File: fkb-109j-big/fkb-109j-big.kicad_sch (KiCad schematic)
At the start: 187 parts

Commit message: start board layout
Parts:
- added D100, D106, D107, D109, D110, D111, D112, D80, D81, D83, D84, D85, D86, D87, D88, D89, D94, D95: 1N4148, Diode_THT:D_DO-35_SOD27_P7.62mm_Horizontal, symbol Diode:1N4148
- added MX_CPSLK1, MX_LSUPR1, MX_RSUPR1: MX-NoLED, Alps_Only:ALPS-1.5U, symbol MX_Alps_Hybrid:MX-NoLED
- added MX_KP0, MX_KP1, MX_KP2, MX_KP3, MX_KP4, MX_KP5, MX_KP6, MX_KP7, MX_KP8, MX_KP9, MX_KPAST1, MX_KPDOT1, MX_KPEQ1, MX_KPFSL1, MX_KPMNS1, MX_KPPLS1, MX_NMLK1: MX-NoLED, Alps_Only:ALPS-1U, symbol MX_Alps_Hybrid:MX-NoLED
- added MX_KPENT1: MX-NoLED, Alps_Only:ALPS-2U, symbol MX_Alps_Hybrid:MX-NoLED
- added MX_LCTRL1, MX_LOPT1, MX_RCTRL1, MX_ROPT1: MX-NoLED, Alps_Only:ALPS-1.25U, symbol MX_Alps_Hybrid:MX-NoLED
- added MX_RSHFT1: MX-NoLED, Alps_Only:ALPS-2.75U, symbol MX_Alps_Hybrid:MX-NoLED
- added MX_RTRN1: MX-NoLED, Alps_Only:ALPS-2.25U, symbol MX_Alps_Hybrid:MX-NoLED
- added MX_SPACE1: MX-NoLED, Alps_Only:ALPS-6.5U, symbol MX_Alps_Hybrid:MX-NoLED
- added MX_SPACE2: MX-NoLED, Alps_Only:ALPS-6.25U, symbol MX_Alps_Hybrid:MX-NoLED
- added R1, R10, R11, R12, R13, R14, R15, R16, R17, R18, R19, R2, R20, R21, R22, R23, R24, R25, R26, R3, R4, R5, R6, R7, R8, R9: R, Resistor_THT:R_Axial_DIN0207_L6.3mm_D2.5mm_P10.16mm_Horizontal, symbol Device:R
- MX_0, MX_1, MX_2, MX_3, MX_4, MX_5, MX_6, MX_7, MX_8, MX_9, MX_F1, MX_F10, MX_F11, MX_F12, MX_F2, MX_F3, MX_F4, MX_F5, MX_F6, MX_F7, MX_F8, MX_F9, MX_KC27, MX_KC28, MX_KC33, MX_KC34, MX_KC35, MX_KC73: footprint (none) -> Alps_Only:ALPS-1U
- MX_A1: renamed from MX_A; footprint (none) -> Alps_Only:ALPS-1U
- MX_B1: renamed from MX_B; footprint (none) -> Alps_Only:ALPS-1U
- MX_BS2: renamed from MX_BS1; footprint Alps_Only:ALPS-1U -> Alps_Only:ALPS-2U
- MX_BSLSH1: renamed from MX_BSLSH; footprint (none) -> Alps_Only:ALPS-1.5U
- MX_C1: renamed from MX_C; footprint (none) -> Alps_Only:ALPS-1U
- MX_CPSLK2: renamed from MX_CPSLK; footprint (none) -> Alps_Only:ALPS-1.75U
- MX_D1: renamed from MX_D; footprint (none) -> Alps_Only:ALPS-1U
- MX_DEL1: renamed from MX_DEL; footprint (none) -> Alps_Only:ALPS-1U
- MX_DOWN1: renamed from MX_DOWN; footprint (none) -> Alps_Only:ALPS-1U
- MX_E1: renamed from MX_E; footprint (none) -> Alps_Only:ALPS-1U
- MX_END1: renamed from MX_END; footprint (none) -> Alps_Only:ALPS-1U
- MX_ENTR1: renamed from MX_ENTR; footprint (none) -> Alps_Only:ALPS-2U
- MX_ESC1: renamed from MX_ESC; footprint (none) -> Alps_Only:ALPS-1U
- MX_F13: renamed from MX_F; footprint (none) -> Alps_Only:ALPS-1U
- MX_G1: renamed from MX_G; footprint (none) -> Alps_Only:ALPS-1U
- MX_H1: renamed from MX_H; footprint (none) -> Alps_Only:ALPS-1U
- MX_HOME1: renamed from MX_HOME; footprint (none) -> Alps_Only:ALPS-1U
- MX_I1: renamed from MX_I; footprint (none) -> Alps_Only:ALPS-1U
- MX_INS1: renamed from MX_INS; footprint (none) -> Alps_Only:ALPS-1U
- MX_J1: renamed from MX_J; footprint (none) -> Alps_Only:ALPS-1U
- MX_K1: renamed from MX_K; footprint (none) -> Alps_Only:ALPS-1U
- MX_KC0C1: renamed from MX_KC0C; footprint (none) -> Alps_Only:ALPS-1U
- MX_KC0D1: renamed from MX_KC0D; footprint (none) -> Alps_Only:ALPS-1U
- MX_KC1A1: renamed from MX_KC1A; footprint (none) -> Alps_Only:ALPS-1U
- MX_KC1B1: renamed from MX_KC1B; footprint (none) -> Alps_Only:ALPS-1U
- MX_KC2B1: renamed from MX_KC2B; footprint (none) -> Alps_Only:ALPS-1U
- MX_KC70, MX_KC79: footprint (none) -> Alps_Only:ALPS-1.25U
- MX_KC7B1: renamed from MX_KC7B; footprint (none) -> Alps_Only:ALPS-1.25U
- MX_KC7D1: renamed from MX_KC7D; footprint (none) -> Alps_Only:ALPS-1U
- MX_L1: renamed from MX_L; footprint (none) -> Alps_Only:ALPS-1U
- MX_LALT1: renamed from MX_LALT; footprint (none) -> Alps_Only:ALPS-1.25U
- MX_LCTRL2: renamed from MX_LCTRL; footprint (none) -> Alps_Only:ALPS-1.5U
- MX_LEFT1: renamed from MX_LEFT; footprint (none) -> Alps_Only:ALPS-1U
- MX_LSHFT1: renamed from MX_LSHFT; footprint (none) -> Alps_Only:ALPS-2.25U
- MX_LWIN1: renamed from MX_LWIN; footprint (none) -> Alps_Only:ALPS-1.25U
- MX_M1: renamed from MX_M; footprint (none) -> Alps_Only:ALPS-1U
- MX_MENU1: renamed from MX_MENU; footprint (none) -> Alps_Only:ALPS-1.25U
- MX_N1: renamed from MX_N; footprint (none) -> Alps_Only:ALPS-1U
- MX_O1: renamed from MX_O; footprint (none) -> Alps_Only:ALPS-1U
- MX_P1: renamed from MX_P; footprint (none) -> Alps_Only:ALPS-1U
- MX_PGDN1: renamed from MX_PGDN; footprint (none) -> Alps_Only:ALPS-1U
- MX_PGUP1: renamed from MX_PGUP; footprint (none) -> Alps_Only:ALPS-1U
- MX_PSBRK1: renamed from MX_PSBRK; footprint (none) -> Alps_Only:ALPS-1U
- MX_PSCRN1: renamed from MX_PSCRN; footprint (none) -> Alps_Only:ALPS-1U
- MX_Q1: renamed from MX_Q; footprint (none) -> Alps_Only:ALPS-1U
- MX_R1: renamed from MX_R; footprint (none) -> Alps_Only:ALPS-1U
- MX_RALT1: renamed from MX_RALT; footprint (none) -> Alps_Only:ALPS-1.25U
- MX_RCTRL2: renamed from MX_CTRL; footprint (none) -> Alps_Only:ALPS-1.5U
- MX_RGHT1: renamed from MX_RGHT; footprint (none) -> Alps_Only:ALPS-1U
- MX_RSHFT2: renamed from MX_RSHFT; footprint (none) -> Alps_Only:ALPS-1.75U
- MX_RWIN1: renamed from MX_RWIN; footprint (none) -> Alps_Only:ALPS-1.25U
- MX_S1: renamed from MX_S; footprint (none) -> Alps_Only:ALPS-1U
- MX_SCRLK1: renamed from MX_SCRLK; footprint (none) -> Alps_Only:ALPS-1U
- MX_SPACE3: renamed from MX_SPACE; footprint (none) -> Alps_Only:ALPS-2.5U
- MX_T1: renamed from MX_T; footprint (none) -> Alps_Only:ALPS-1U
- MX_TAB1: renamed from MX_TAB; footprint (none) -> Alps_Only:ALPS-1.5U
- MX_TILDE1: renamed from MX_TILDE; footprint (none) -> Alps_Only:ALPS-1U
- MX_U1: renamed from MX_U; footprint (none) -> Alps_Only:ALPS-1U
- MX_UP1: renamed from MX_UP; footprint (none) -> Alps_Only:ALPS-1U
- MX_V1: renamed from MX_V; footprint (none) -> Alps_Only:ALPS-1U
- MX_W1: renamed from MX_W; footprint (none) -> Alps_Only:ALPS-1U
- MX_X1: renamed from MX_X; footprint (none) -> Alps_Only:ALPS-1U
- MX_Y1: renamed from MX_Y; footprint (none) -> Alps_Only:ALPS-1U
- MX_Z1: renamed from MX_Z; footprint (none) -> Alps_Only:ALPS-1U
- renumbered MX_BS2 to MX_BS1
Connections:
- net COL2: now reaches MX_S1.1 (COL)
- net COL2: now also MX_2.1 (COL), MX_LALT1.1 (COL), MX_W1.1 (COL), MX_X1.1 (COL), MX_LSUPR1.2 (ROW), R2.2
- net at D97.1 (K): now also D103.1 (K), D91.1 (K), R17.2
- net ROW4: now reaches D53.1 (K)
- net ROW4: now also D17.1 (K), D19.1 (K), D21.1 (K), D23.1 (K), D29.1 (K), D35.1 (K), D41.1 (K), D47.1 (K), D59.1 (K), D65.1 (K), D71.1 (K), D77.1 (K), D82.1 (K), R20.1
- net COL9: now reaches MX_O1.1 (COL)
- net COL9: now also MX_9.1 (COL), MX_KC34.1 (COL), MX_L1.1 (COL), MX_MENU1.1 (COL), MX_ROPT1.2 (ROW), R9.2
- net ROW5: now reaches D24.1 (K)
- net ROW5: now also D18.1 (K), D20.1 (K), D22.1 (K), D30.1 (K), D36.1 (K), D42.1 (K), D48.1 (K), D54.1 (K), D60.1 (K), D66.1 (K), R22.1
- net ROW3: now reaches D34.1 (K)
- net ROW3: now also D10.1 (K), D12.1 (K), D14.1 (K), D16.1 (K), D28.1 (K), D40.1 (K), D46.1 (K), D52.1 (K), D58.1 (K), D64.1 (K), D70.1 (K), D72.1 (K), D76.1 (K), R21.1
- net COL13: now reaches MX_BS1.1 (COL), MX_BS2.1 (COL)
- net COL13: now also MX_BSLSH1.1 (COL), MX_ENTR1.1 (COL), MX_KC7D1.1 (COL), MX_RTRN1.1 (COL), R13.2
- net ROW1: now reaches D68.1 (K)
- net ROW1: now also D26.1 (K), D32.1 (K), D38.1 (K), D44.1 (K), D5.1 (K), D50.1 (K), D56.1 (K), D6.1 (K), D62.1 (K), D7.1 (K), D74.1 (K), D79.1 (K), D8.1 (K), R18.1
- net COL10: now reaches MX_P1.1 (COL)
- net COL10: now also MX_0.1 (COL), MX_KC27.1 (COL), MX_KC35.1 (COL), MX_RCTRL2.1 (COL), MX_RCTRL1.1 (COL), R10.2
- net ROW0: now reaches D3.1 (K)
- net ROW0: now also D1.1 (K), D2.1 (K), D25.1 (K), D31.1 (K), D37.1 (K), D4.1 (K), D43.1 (K), D49.1 (K), D55.1 (K), D61.1 (K), D67.1 (K), D73.1 (K), R17.1
- net COL11: now reaches MX_KC73.1 (COL)
- net COL11: now also MX_KC0C1.1 (COL), MX_KC1A1.1 (COL), MX_KC28.1 (COL), R11.2
- net at MX_F6.1 (COL): now also R7.1
- net ROW2: now reaches D13.1 (K)
- net ROW2: now also D11.1 (K), D15.1 (K), D27.1 (K), D33.1 (K), D39.1 (K), D45.1 (K), D51.1 (K), D57.1 (K), D63.1 (K), D69.1 (K), D75.1 (K), D78.1 (K), D9.1 (K), R19.1
- net COL7: now reaches MX_U1.1 (COL)
- net COL7: now also MX_7.1 (COL), MX_J1.1 (COL), MX_M1.1 (COL), MX_RALT1.1 (COL), R7.2
- net at D96.1 (K): now also D102.1 (K), D108.1 (K), R22.2, R26.1
- net COL4: now reaches MX_V1.1 (COL)
- net COL4: now also MX_4.1 (COL), MX_F13.1 (COL), MX_R1.1 (COL), MX_SPACE3.1 (COL), MX_SPACE1.1 (COL), MX_SPACE2.1 (COL), R4.2
- net at D20.2 (A), MX_LWIN1.2 (ROW): now also MX_LOPT1.1 (COL)
- net COL1: now reaches MX_LWIN1.1 (COL)
- net COL1: now also MX_1.1 (COL), MX_A1.1 (COL), MX_Q1.1 (COL), MX_Z1.1 (COL), MX_LOPT1.2 (ROW)
- net COL6: now reaches MX_H1.1 (COL)
- net COL6: now also MX_6.1 (COL), MX_KC70.1 (COL), MX_N1.1 (COL), MX_Y1.1 (COL), R6.2
- net at D30.2 (A), MX_SPACE3.2 (ROW): now also MX_SPACE1.2 (ROW), MX_SPACE2.2 (ROW)
- net COL0: now reaches MX_TAB1.1 (COL)
- net COL0: now also MX_CPSLK2.1 (COL), MX_LCTRL2.1 (COL), MX_LSHFT1.1 (COL), MX_TILDE1.1 (COL), MX_CPSLK1.1 (COL), MX_LCTRL1.1 (COL), R1.2
- net at D93.1 (K): now also D105.1 (K), D99.1 (K), R19.2, R24.1
- net COL8: now reaches MX_I1.1 (COL)
- net COL8: now also MX_8.1 (COL), MX_K1.1 (COL), MX_KC33.1 (COL), MX_RWIN1.1 (COL), MX_RSUPR1.2 (ROW), R8.2
- net at D82.2 (A), MX_ENTR1.2 (ROW): now also MX_RTRN1.2 (ROW)
- net COL5: now reaches MX_5.1 (COL)
- net COL5: now also MX_B1.1 (COL), MX_G1.1 (COL), MX_KC79.1 (COL), MX_T1.1 (COL), R5.2
- net COL12: now reaches MX_KC0D1.1 (COL)
- net COL12: now also MX_KC1B1.1 (COL), MX_KC2B1.1 (COL), MX_RSHFT2.1 (COL), MX_RSHFT1.1 (COL), R12.2
- net at MX_MENU1.2 (ROW): now also D60.2 (A), MX_ROPT1.1 (COL); no longer D48.2 (A)
- net at D77.2 (A), MX_RSHFT2.2 (ROW): now also MX_RSHFT1.2 (ROW)
- net at D22.2 (A), MX_LALT1.2 (ROW): now also MX_LSUPR1.1 (COL)
- net at MX_PSCRN1.1 (COL): now also R14.1
- net at D54.2 (A), MX_RWIN1.2 (ROW): now also MX_RSUPR1.1 (COL)
- net at MX_F12.1 (COL): now also R13.1
- net at MX_F5.1 (COL): now also R6.1
- net COL14: now reaches MX_DEL1.1 (COL)
- net COL14: now also MX_INS1.1 (COL), MX_LEFT1.1 (COL), R14.2
- net at MX_F10.1 (COL): now also R11.1
- net at D98.1 (K): now also D104.1 (K), D92.1 (K), R18.2, R23.1
- net at MX_F4.1 (COL): now also R5.1
- net at D18.2 (A), MX_LCTRL2.2 (ROW): now also MX_LCTRL1.2 (ROW)
- net at MX_F8.1 (COL): now also R9.1
- net at MX_ESC1.1 (COL): now also R1.1
- net at MX_F7.1 (COL): now also R8.1
- net COL16: now reaches MX_PGDN1.1 (COL)
- net COL16: now also MX_PGUP1.1 (COL), MX_RGHT1.1 (COL), R16.2
- net at D66.2 (A), MX_RCTRL2.2 (ROW): now also MX_RCTRL1.2 (ROW)
- net at MX_F9.1 (COL): now also R10.1
- net at MX_RALT1.2 (ROW): now also D48.2 (A); no longer D60.2 (A)
- net COL15: now reaches MX_HOME1.1 (COL)
- net COL15: now also MX_DOWN1.1 (COL), MX_END1.1 (COL), MX_UP1.1 (COL), R15.2
- net at D101.1 (K): now also R20.2, R25.1
- net at MX_SCRLK1.1 (COL): now also R15.1
- net COL3: now reaches MX_KC7B1.1 (COL)
- net COL3: now also MX_3.1 (COL), MX_C1.1 (COL), MX_D1.1 (COL), MX_E1.1 (COL), R3.2
- net at MX_F1.1 (COL): now also R2.1
- net at MX_F3.1 (COL): now also R4.1
- net at MX_F11.1 (COL): now also R12.1
- net at D10.2 (A), MX_CPSLK2.2 (ROW): now also MX_CPSLK1.2 (ROW)
- net at MX_F2.1 (COL): now also R3.1
- net at MX_PSBRK1.1 (COL): now also R16.1
- new net: D100.1 (K), D111.1 (K), D83.1 (K), D88.1 (K), R21.2
- new net: D106.1 (K), D112.1 (K), D84.1 (K), D89.1 (K), R25.2
- new net: D84.2 (A), MX_KP1.2 (ROW)
- new net: D81.2 (A), MX_KP7.2 (ROW)
- new net: D109.1 (K), D80.1 (K), D86.1 (K), D94.1 (K), R23.2
- new net: D89.2 (A), MX_KP2.2 (ROW)
- new net: D107.2 (A), MX_KPDOT1.2 (ROW)
- new net: D80.2 (A), MX_NMLK1.2 (ROW)
- new net: D107.1 (K), D85.1 (K), R26.2
- new net: D85.2 (A), MX_KP0.2 (ROW)
- new net: D110.1 (K), D81.1 (K), D87.1 (K), D95.1 (K), R24.2
- new net: D110.2 (A), MX_KPMNS1.2 (ROW)
- new net: D112.2 (A), MX_KPENT1.2 (ROW)
- new net: D86.2 (A), MX_KPEQ1.2 (ROW)
- new net: D88.2 (A), MX_KP5.2 (ROW)
- new net: D111.2 (A), MX_KPPLS1.2 (ROW)
- new net: D83.2 (A), MX_KP4.2 (ROW)
- new net: D95.2 (A), MX_KP9.2 (ROW)
- new net: D100.2 (A), MX_KP6.2 (ROW)
- new net: D94.2 (A), MX_KPFSL1.2 (ROW)
- new net: D87.2 (A), MX_KP8.2 (ROW)
- new net: D109.2 (A), MX_KPAST1.2 (ROW)
- new net: D106.2 (A), MX_KP3.2 (ROW)
- new net COL17: MX_KP0.1 (COL), MX_KP1.1 (COL), MX_KP4.1 (COL), MX_KP7.1 (COL), MX_NMLK1.1 (COL)
- new net COL18: MX_KP2.1 (COL), MX_KP5.1 (COL), MX_KP8.1 (COL), MX_KPEQ1.1 (COL)
- new net COL19: MX_KP3.1 (COL), MX_KP6.1 (COL), MX_KP9.1 (COL), MX_KPDOT1.1 (COL), MX_KPFSL1.1 (COL)
- new net COL20: MX_KPAST1.1 (COL), MX_KPENT1.1 (COL), MX_KPMNS1.1 (COL), MX_KPPLS1.1 (COL)
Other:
- moved on the sheet: D101, D102, D108, D2, D25, D3, D31, D37, D4, D43, D49, D55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

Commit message: continue layout
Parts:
- added MX_KPPLS2: MX-NoLED, Alps_Only:ALPS-2U, symbol MX_Alps_Hybrid:MX-NoLED
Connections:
- net COL20: now also MX_KPPLS2.1 (COL)
- net at D111.2 (A), MX_KPPLS1.2 (ROW): now also MX_KPPLS2.2 (ROW)
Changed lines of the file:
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@@
   (junction (at 86.36 138.43) (diameter 0) (color 0 0 0 0)
   )
+  (junction (at 307.34 102.87) (diameter 0) (color 0 0 0 0)
+  )
   (junction (at 193.04 105.41) (diameter 0) (color 0 0 0 0)
   )
@@
   (junction (at 40.64 125.73) (diameter 0) (color 0 0 0 0)
   )
+  (junction (at 302.26 110.49) (diameter 0) (color 0 0 0 0)
+  )
   (junction (at 231.14 85.09) (diameter 0) (color 0 0 0 0)
   )
@@
     (stroke (width 0) (type default))
   )
-  (wire (pts (xy 307.34 85.09) (xy 307.34 105.41))
+  (wire (pts (xy 307.34 85.09) (xy 307.34 102.87))
     (stroke (width 0) (type default))
   )
@@
     (stroke (width 0) (type default))
   )
+  (wire (pts (xy 299.72 107.95) (xy 299.72 110.49))
+    (stroke (width 0) (type default))
+  )
   (wire (pts (xy 25.4 102.87) (xy 27.94 102.87))
     (stroke (width 0) (type default))
@@
     (stroke (width 0) (type default))
   )
+  (wire (pts (xy 304.8 102.87) (xy 307.34 102.87))
+    (stroke (width 0) (type default))
+  )
   (wire (pts (xy 40.64 140.97) (xy 40.64 146.05))
     (stroke (width 0) (type default))
@@
     (stroke (width 0) (type default))
   )
+  (wire (pts (xy 299.72 110.49) (xy 302.26 110.49))
+    (stroke (width 0) (type default))
+  )
   (wire (pts (xy 66.04 25.4) (xy 66.04 43.18))
     (stroke (width 0) (type default))
@@
     (stroke (width 0) (type default))
   )
+  (wire (pts (xy 307.34 102.87) (xy 307.34 105.41))
+    (stroke (width 0) (type default))
+  )
   (wire (pts (xy 116.84 50.8) (xy 116.84 64.77))
     (stroke (width 0) (type default))
@@
         )
       )
+    )
+  )
+  (symbol (lib_id "MX_Alps_Hybrid:MX-NoLED") (at 300.99 104.14 0) (unit 1)
+    (in_bom yes) (on_board yes) (dnp no) (fields_autoplaced)
+    (property "Reference" "MX_KPPLS2" (at 301.8732 97.79 0)
+      (effects (font (size 1.524 1.524)))
+    )
+    (property "Value" "MX-NoLED" (at 301.8732 100.33 0)
+      (effects (font (size 0.508 0.508)))
+    )
+    (property "Footprint" "Alps_Only:ALPS-2U" (at 285.115 104.775 0)
+      (effects (font (size 1.524 1.524)) hide)
+    )
+    (property "Datasheet" "" (at 285.115 104.775 0)
+      (effects (font (size 1.524 1.524)) hide)
+    )
+    (pin "1")
+    (pin "2")
+    (instances
+      (project "fkb-109j-big"
+        (path "/b3d18fbb-85f6-4085-bc49-223707581c3b"
+          (reference "MX_KPPLS2") (unit 1)
+        )
+      )

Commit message: fix footprint
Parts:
- MX_KP0: footprint Alps_Only:ALPS-1U -> Alps_Only:ALPS-2U
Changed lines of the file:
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@@
       (effects (font (size 0.508 0.508)))
     )
-    (property "Footprint" "Alps_Only:ALPS-1U" (at 249.555 147.955 0)
+    (property "Footprint" "Alps_Only:ALPS-2U" (at 249.555 147.955 0)
       (effects (font (size 1.524 1.524)) hide)
     )

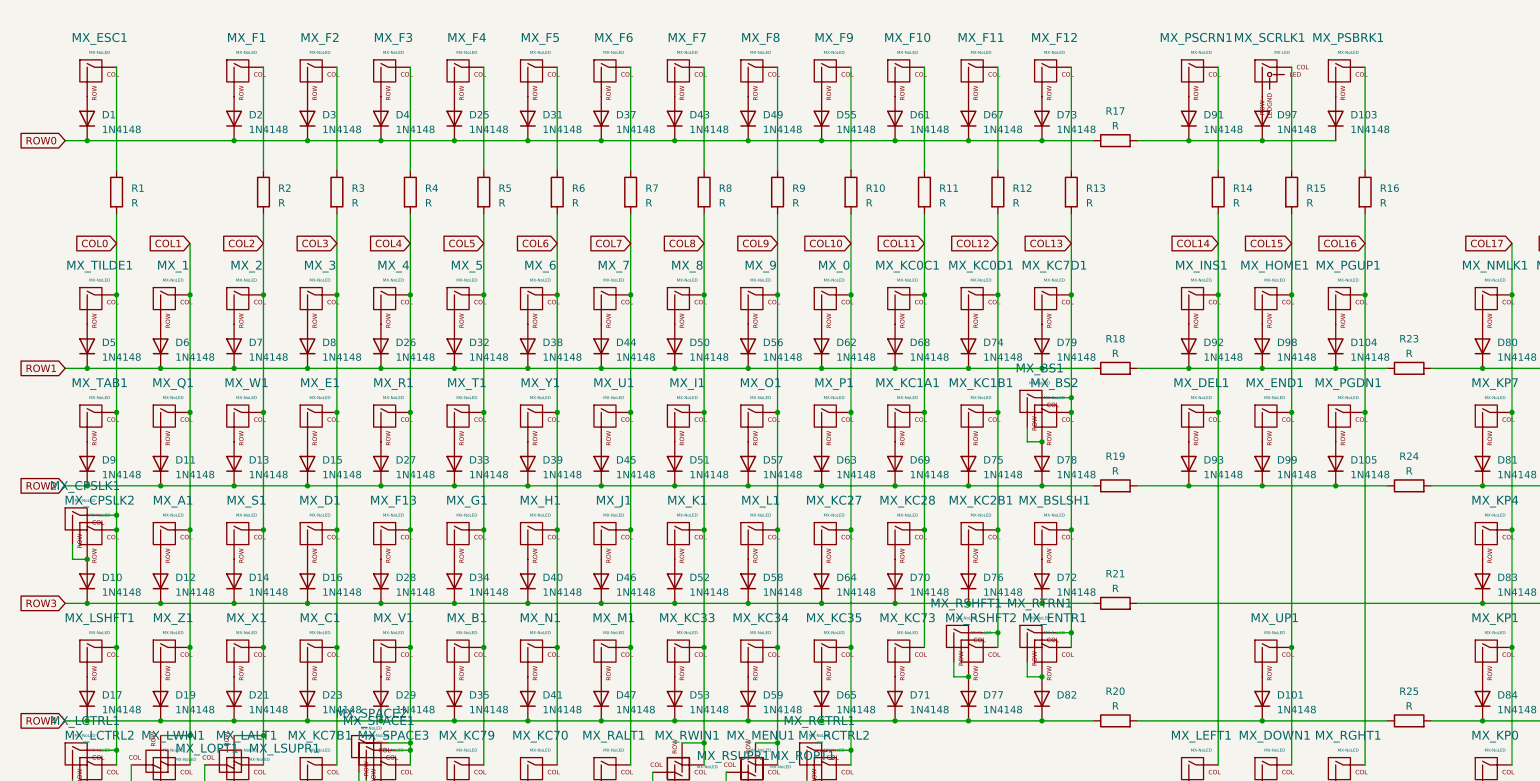
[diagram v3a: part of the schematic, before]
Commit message: finish preliminary layout
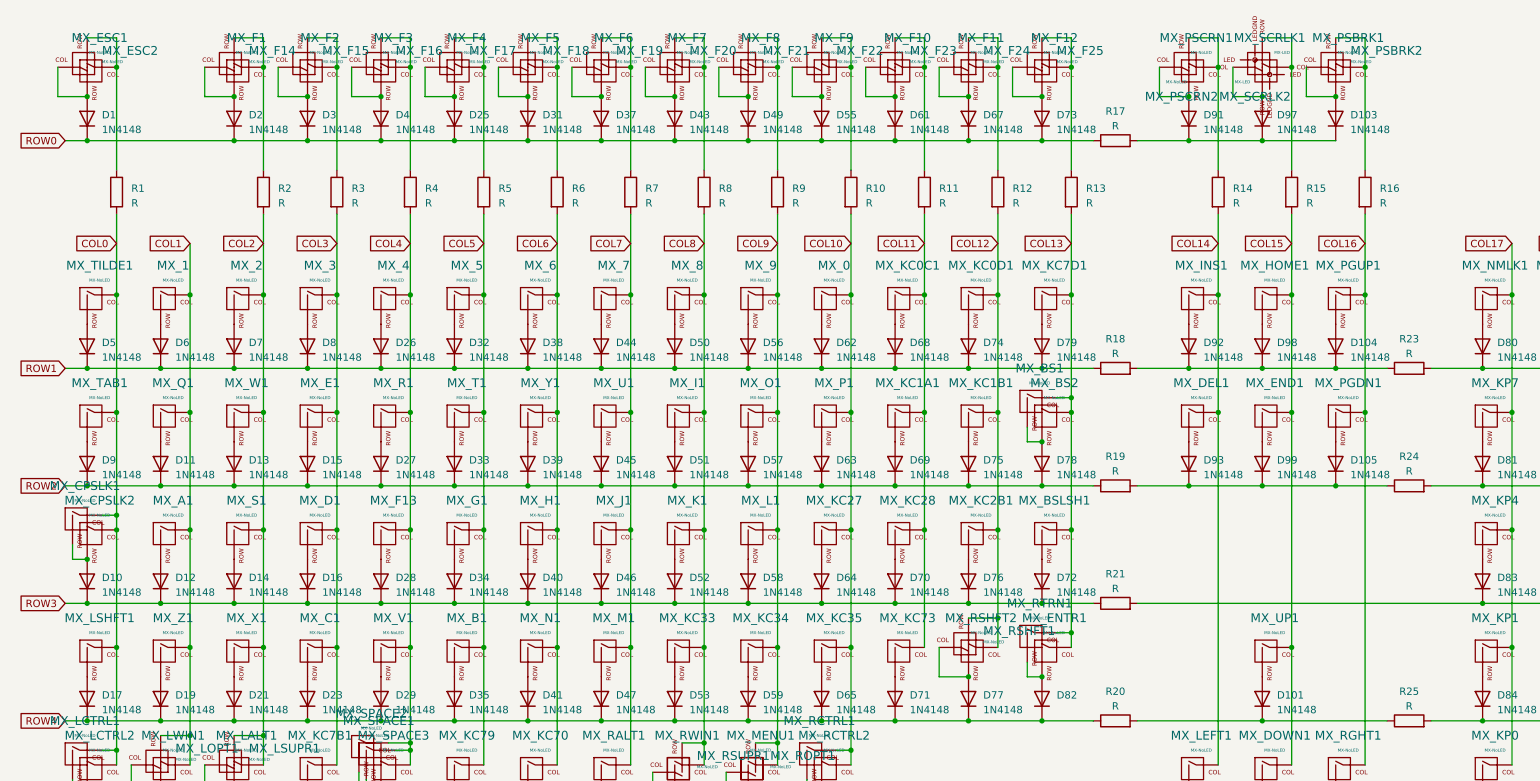
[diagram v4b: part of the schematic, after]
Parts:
- added MX_ESC2, MX_F14, MX_F15, MX_F16, MX_F17, MX_F18, MX_F19, MX_F20, MX_F21, MX_F22, MX_F23, MX_F24, MX_F25, MX_PSBRK2, MX_PSCRN2: MX-NoLED, Alps_Only:ALPS-1U, symbol MX_Alps_Hybrid:MX-NoLED
- added MX_SCRLK2: MX-LED, Alps_Only:ALPS-1U, symbol MX_Alps_Hybrid:MX-LED
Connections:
- net COL12: now also MX_RSHFT1.2 (ROW); no longer MX_RSHFT1.1 (COL)
- net at D97.2 (A), MX_SCRLK1.2 (ROW): now also MX_SCRLK2.1 (COL)
- net at MX_F6.1 (COL), R7.1: now also MX_F19.2 (ROW)
- net at MX_F11.1 (COL), R12.1: now also MX_F24.2 (ROW)
- net at MX_F7.1 (COL), R8.1: now also MX_F20.2 (ROW)
- net at MX_SCRLK1.1 (COL), R15.1: now also MX_SCRLK2.2 (ROW)
- net at D3.2 (A), MX_F2.2 (ROW): now also MX_F15.1 (COL)
- net at D37.2 (A), MX_F6.2 (ROW): now also MX_F19.1 (COL)
- net at D25.2 (A), MX_F4.2 (ROW): now also MX_F17.1 (COL)
- net at D4.2 (A), MX_F3.2 (ROW): now also MX_F16.1 (COL)
- net at D55.2 (A), MX_F9.2 (ROW): now also MX_F22.1 (COL)
- net at MX_PSCRN1.1 (COL), R14.1: now also MX_PSCRN2.2 (ROW)
- net at D91.2 (A), MX_PSCRN1.2 (ROW): now also MX_PSCRN2.1 (COL)
- net at MX_F1.1 (COL), R2.1: now also MX_F14.2 (ROW)
- net at D61.2 (A), MX_F10.2 (ROW): now also MX_F23.1 (COL)
- net at D77.2 (A), MX_RSHFT2.2 (ROW): now also MX_RSHFT1.1 (COL); no longer MX_RSHFT1.2 (ROW)
- net at MX_F5.1 (COL), R6.1: now also MX_F18.2 (ROW)
- net at MX_F12.1 (COL), R13.1: now also MX_F25.2 (ROW)
- net at D73.2 (A), MX_F12.2 (ROW): now also MX_F25.1 (COL)
- net at D31.2 (A), MX_F5.2 (ROW): now also MX_F18.1 (COL)
- net at D103.2 (A), MX_PSBRK1.2 (ROW): now also MX_PSBRK2.1 (COL)
- net at MX_F8.1 (COL), R9.1: now also MX_F21.2 (ROW)
- net at MX_F10.1 (COL), R11.1: now also MX_F23.2 (ROW)
- net at MX_F4.1 (COL), R5.1: now also MX_F17.2 (ROW)
- net at D67.2 (A), MX_F11.2 (ROW): now also MX_F24.1 (COL)
- net at MX_F2.1 (COL), R3.1: now also MX_F15.2 (ROW)
- net at MX_F9.1 (COL), R10.1: now also MX_F22.2 (ROW)
- net at D49.2 (A), MX_F8.2 (ROW): now also MX_F21.1 (COL)
- net at MX_ESC1.1 (COL), R1.1: now also MX_ESC2.2 (ROW)
- net at D1.2 (A), MX_ESC1.2 (ROW): now also MX_ESC2.1 (COL)
- net at D43.2 (A), MX_F7.2 (ROW): now also MX_F20.1 (COL)
- net at MX_PSBRK1.1 (COL), R16.1: now also MX_PSBRK2.2 (ROW)
- net at D2.2 (A), MX_F1.2 (ROW): now also MX_F14.1 (COL)
- net at MX_F3.1 (COL), R4.1: now also MX_F16.2 (ROW)
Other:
- moved on the sheet: MX_RSHFT1

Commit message: start moving diodes
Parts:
- added MX_BSLSH2: MX-NoLED, Alps_Only:ALPS-1U, symbol MX_Alps_Hybrid:MX-NoLED
- added MX_LSHFT2: MX-NoLED, Alps_Only:ALPS-1.25U, symbol MX_Alps_Hybrid:MX-NoLED
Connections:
- net COL0: now also MX_LSHFT2.1 (COL)
- net COL13: now also MX_BSLSH2.2 (ROW)
- net at D17.2 (A), MX_LSHFT1.2 (ROW): now also MX_LSHFT2.2 (ROW)
- net at D72.2 (A), MX_BSLSH1.2 (ROW): now also MX_BSLSH2.1 (COL)
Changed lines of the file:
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@@
   (junction (at 129.54 85.09) (diameter 0) (color 0 0 0 0)
   )
+  (junction (at 193.04 100.33) (diameter 0) (color 0 0 0 0)
+  )
   (junction (at 116.84 64.77) (diameter 0) (color 0 0 0 0)
   )
@@
   (junction (at 231.14 25.4) (diameter 0) (color 0 0 0 0)
   )
+  (junction (at 22.86 130.81) (diameter 0) (color 0 0 0 0)
+  )
   (junction (at 40.64 125.73) (diameter 0) (color 0 0 0 0)
   )
@@
   (junction (at 22.86 138.43) (diameter 0) (color 0 0 0 0)
   )
+  (junction (at 187.96 110.49) (diameter 0) (color 0 0 0 0)
+  )
   (junction (at 129.54 105.41) (diameter 0) (color 0 0 0 0)
   )
   (junction (at 78.74 85.09) (diameter 0) (color 0 0 0 0)
   )
+  (junction (at 27.94 123.19) (diameter 0) (color 0 0 0 0)
+  )
   (junction (at 175.26 38.1) (diameter 0) (color 0 0 0 0)
   )
@@
     (stroke (width 0) (type default))
   )
+  (wire (pts (xy 20.32 128.27) (xy 20.32 130.81))
+    (stroke (width 0) (type default))
+  )
   (wire (pts (xy 27.94 102.87) (xy 27.94 105.41))
     (stroke (width 0) (type default))
@@
     (stroke (width 0) (type default))
   )
-  (wire (pts (xy 27.94 105.41) (xy 27.94 125.73))
+  (wire (pts (xy 27.94 105.41) (xy 27.94 123.19))
     (stroke (width 0) (type default))
   )
@@
     (stroke (width 0) (type default))
   )
+  (wire (pts (xy 27.94 123.19) (xy 27.94 125.73))
+    (stroke (width 0) (type default))
+  )
   (wire (pts (xy 175.26 77.47) (xy 187.96 77.47))
     (stroke (width 0) (type default))
@@
     (stroke (width 0) (type default))
   )
+  (wire (pts (xy 182.88 110.49) (xy 187.96 110.49))
+    (stroke (width 0) (type default))
+  )
   (wire (pts (xy 104.14 85.09) (xy 104.14 105.41))
     (stroke (width 0) (type default))
@@
     (stroke (width 0) (type default))
   )
-  (wire (pts (xy 193.04 85.09) (xy 193.04 105.41))
+  (wire (pts (xy 193.04 85.09) (xy 193.04 100.33))
     (stroke (width 0) (type default))
   )
@@
     (stroke (width 0) (type default))
   )
+  (wire (pts (xy 182.88 105.41) (xy 182.88 110.49))
+    (stroke (width 0) (type default))
+  )
   (wire (pts (xy 238.76 77.47) (xy 247.65 77.47))
     (stroke (width 0) (type default))
@@
     (stroke (width 0) (type default))
   )
+  (wire (pts (xy 193.04 100.33) (xy 193.04 105.41))
+    (stroke (width 0) (type default))
+  )
   (wire (pts (xy 180.34 85.09) (xy 180.34 105.41))
     (stroke (width 0) (type default))
@@
     (stroke (width 0) (type default))
   )
+  (wire (pts (xy 25.4 123.19) (xy 27.94 123.19))
+    (stroke (width 0) (type default))
+  )
   (wire (pts (xy 104.14 105.41) (xy 104.14 125.73))
     (stroke (width 0) (type default))
@@
     (stroke (width 0) (type default))
   )
+  (wire (pts (xy 20.32 130.81) (xy 22.86 130.81))
+    (stroke (width 0) (type default))
+  )
   (wire (pts (xy 137.16 118.11) (xy 149.86 118.11))
     (stroke (width 0) (type default))
@@
     (stroke (width 0) (type default))
   )
+  (wire (pts (xy 187.96 100.33) (xy 193.04 100.33))
+    (stroke (width 0) (type default))
+  )
   (wire (pts (xy 73.66 97.79) (xy 86.36 97.79))
     (stroke (width 0) (type default))
@@
     )
   )
+  (symbol (lib_id "MX_Alps_Hybrid:MX-NoLED") (at 21.59 124.46 0) (unit 1)
+    (in_bom yes) (on_board yes) (dnp no) (fields_autoplaced)
+    (property "Reference" "MX_LSHFT2" (at 22.4732 118.11 0)
+      (effects (font (size 1.524 1.524)))
+    )
+    (property "Value" "MX-NoLED" (at 22.4732 120.65 0)
+      (effects (font (size 0.508 0.508)))
+    )
+    (property "Footprint" "Alps_Only:ALPS-1.25U" (at 5.715 125.095 0)
+      (effects (font (size 1.524 1.524)) hide)
+    )
+    (property "Datasheet" "" (at 5.715 125.095 0)
+      (effects (font (size 1.524 1.524)) hide)
+    )
+    (pin "1")
+    (pin "2")
+    (instances
+      (project "fkb-109j-big"
+        (path "/b3d18fbb-85f6-4085-bc49-223707581c3b"
+          (reference "MX_LSHFT2") (unit 1)
+        )
+      )
+    )
+  )
   (symbol (lib_id "Diode:1N4148") (at 60.96 134.62 90) (unit 1)
     (in_bom yes) (on_board yes) (dnp no)
@@
         )
       )
+    )
+  )
+  (symbol (lib_id "MX_Alps_Hybrid:MX-NoLED") (at 186.69 104.14 180) (unit 1)
+    (in_bom yes) (on_board yes) (dnp no) (fields_autoplaced)
+    (property "Reference" "MX_BSLSH2" (at 190.5 102.564 0)
+      (effects (font (size 1.524 1.524)) (justify right))
+    )
+    (property "Value" "MX-NoLED" (at 190.5 104.469 0)
+      (effects (font (size 0.508 0.508)) (justify right))
+    )
+    (property "Footprint" "Alps_Only:ALPS-1U" (at 202.565 103.505 0)
+      (effects (font (size 1.524 1.524)) hide)
+    )
+    (property "Datasheet" "" (at 202.565 103.505 0)
+      (effects (font (size 1.524 1.524)) hide)
+    )
+    (pin "1")
+    (pin "2")
+    (instances
+      (project "fkb-109j-big"
+        (path "/b3d18fbb-85f6-4085-bc49-223707581c3b"
+          (reference "MX_BSLSH2") (unit 1)
+        )
+      )
